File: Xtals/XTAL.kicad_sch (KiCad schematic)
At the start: 4 parts

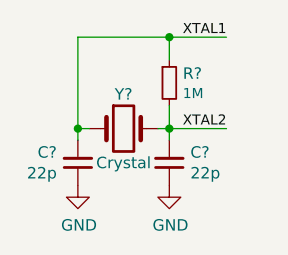
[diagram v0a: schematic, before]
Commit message: Fix grid alignment and update to KiCad 9
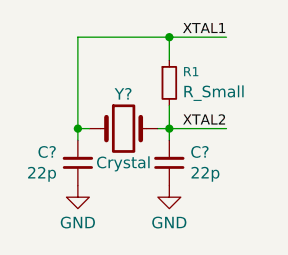
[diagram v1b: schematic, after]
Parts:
- removed R?: 1M, symbol Device:R_Small
- added R1: R_Small, symbol Device:R_Small
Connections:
- net XTAL1: now also R1.1
- net XTAL2: now also R1.2
